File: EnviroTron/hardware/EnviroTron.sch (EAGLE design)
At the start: 35 parts, among them U2 MCP3221

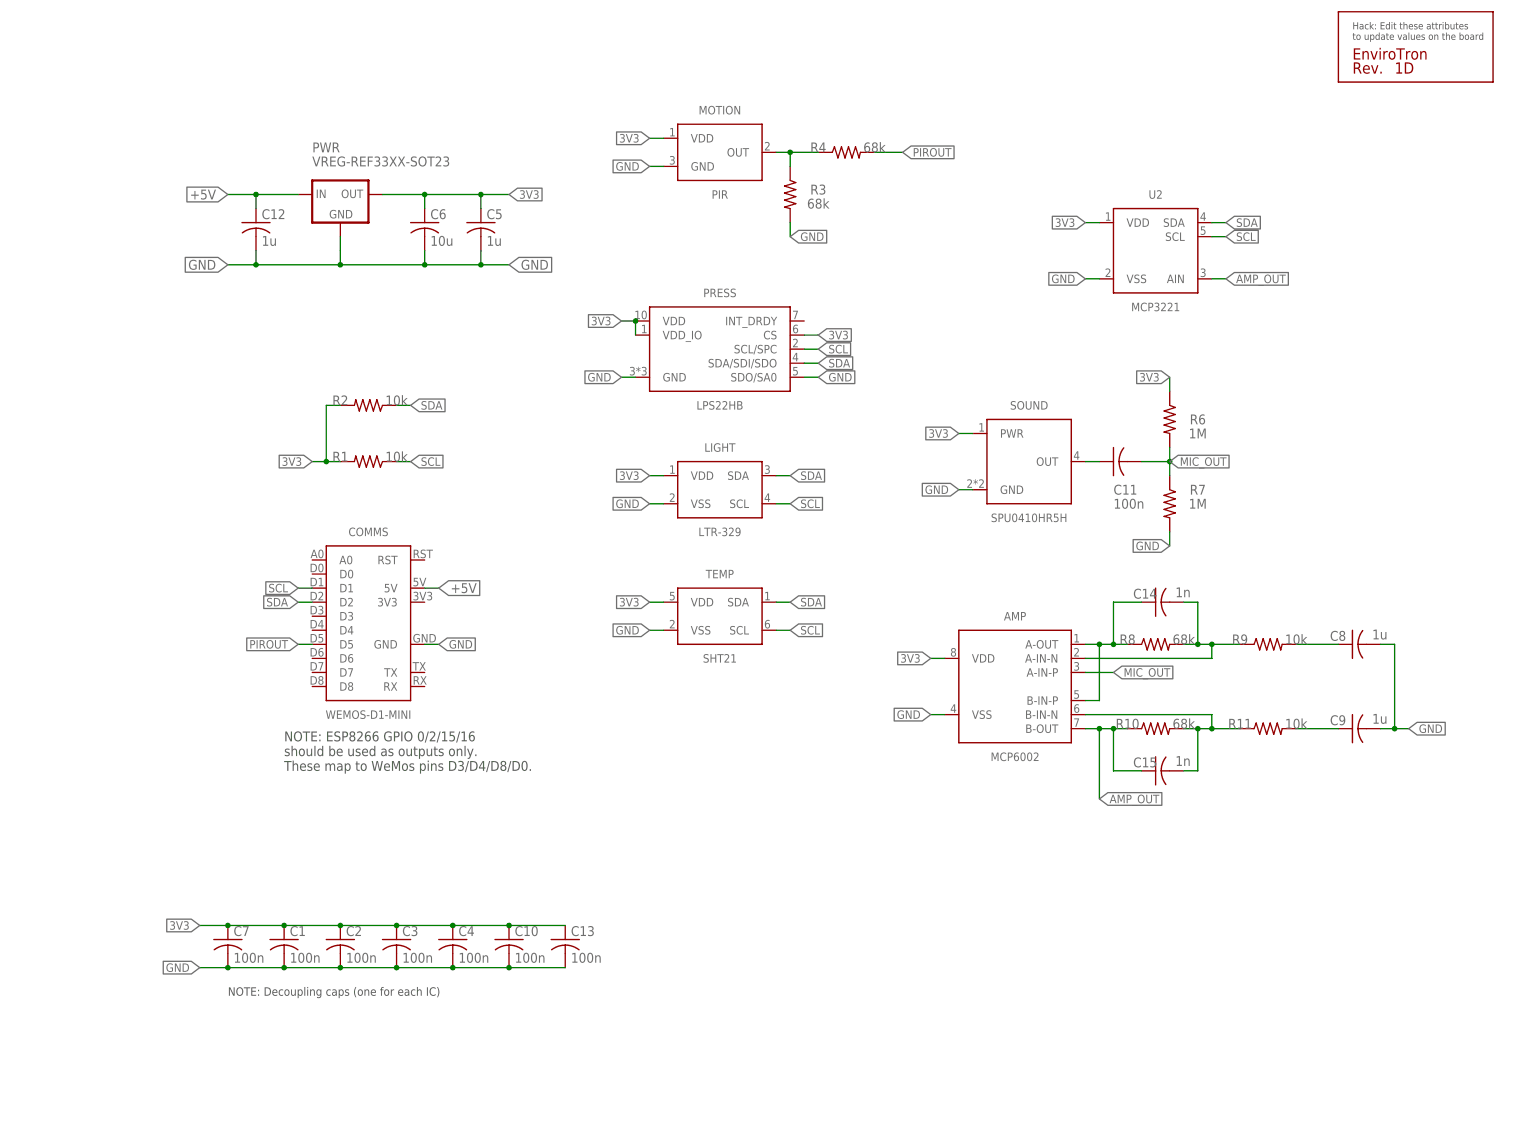
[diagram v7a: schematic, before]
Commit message: Changed mic to new part. Added Pi filter for analog voltage rail.
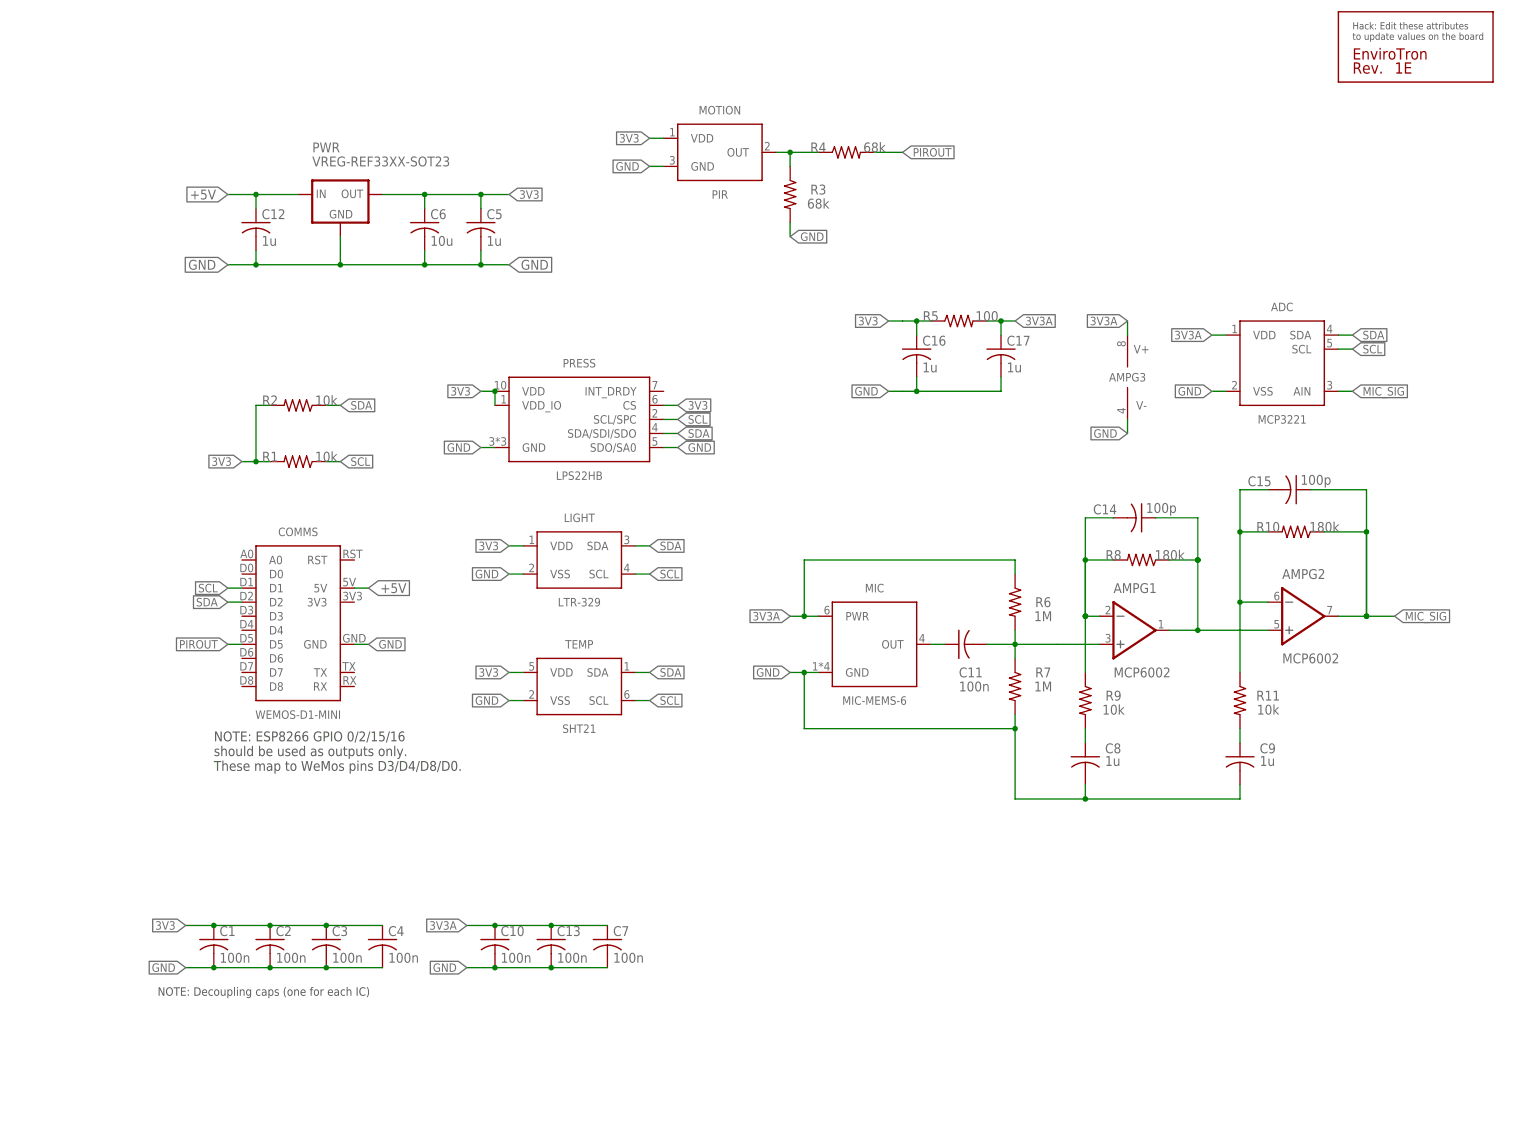
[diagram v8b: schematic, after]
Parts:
- removed SOUND: SPU0410HR5H, EnviroTron:SPU0410HR5H
- removed U2: MCP3221, EnviroTron:MCP3221
- added ADC: MCP3221, EnviroTron:MCP3221
- added C16, C17: 1u, EnviroTron:C-USC0603
- added MIC: MIC-MEMS-6, EnviroTron:MIC-MEMS-6
- added R5: 100, EnviroTron:R-US_R0603
- C14, C15: value 1n -> 100p
- R10, R8: value 68k -> 180k
- U$1: REV 1D -> 1E
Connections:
- removed net AMP_OUT: AMP.B-OUT, C15.1, R10.1, U2.AIN
- new net 3V3A: ADC.VDD, AMPG3.V+, C10.1, C13.1, C17.1, C7.1, MIC.PWR, R5.2, R6.1
- new net MIC_SIG: ADC.AIN, AMPG2.OUT, C15.1, R10.1
- net 3V3: now also C16.1, R5.1; no longer AMP.VDD, C10.1, C13.1, C7.1, R6.1, SOUND.PWR, U2.VDD
- net GND: now also ADC.VSS, AMPG3.V-, C16.2, C17.2, MIC.GND; no longer AMP.VSS, SOUND.GND, U2.VSS
- net MIC_OUT: now also AMPG1.+IN; no longer AMP.A-IN-P
- net N$2: now also AMPG1.OUT, AMPG2.+IN; no longer AMP.A-OUT, AMP.B-IN-P
- net N$6: now also AMPG1.-IN; no longer AMP.A-IN-N
- net N$8: now also MIC.OUT; no longer SOUND.OUT
- net N$9: now also AMPG2.-IN; no longer AMP.B-IN-N
- net SCL: now also ADC.SCL; no longer U2.SCL
- net SDA: now also ADC.SDA; no longer U2.SDA
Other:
- moved on the sheet: C1, C10, C11, C13, C14, C15, C2, C3, C4, C7, C8, C9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
